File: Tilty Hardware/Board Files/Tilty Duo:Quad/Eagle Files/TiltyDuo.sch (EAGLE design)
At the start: 36 parts, among them U1 HMC5883LSMD, U2 HC-09_BREAKOUT, U3 MPL3115A2LGA8, U4 LM2931, U5 MPU-6050

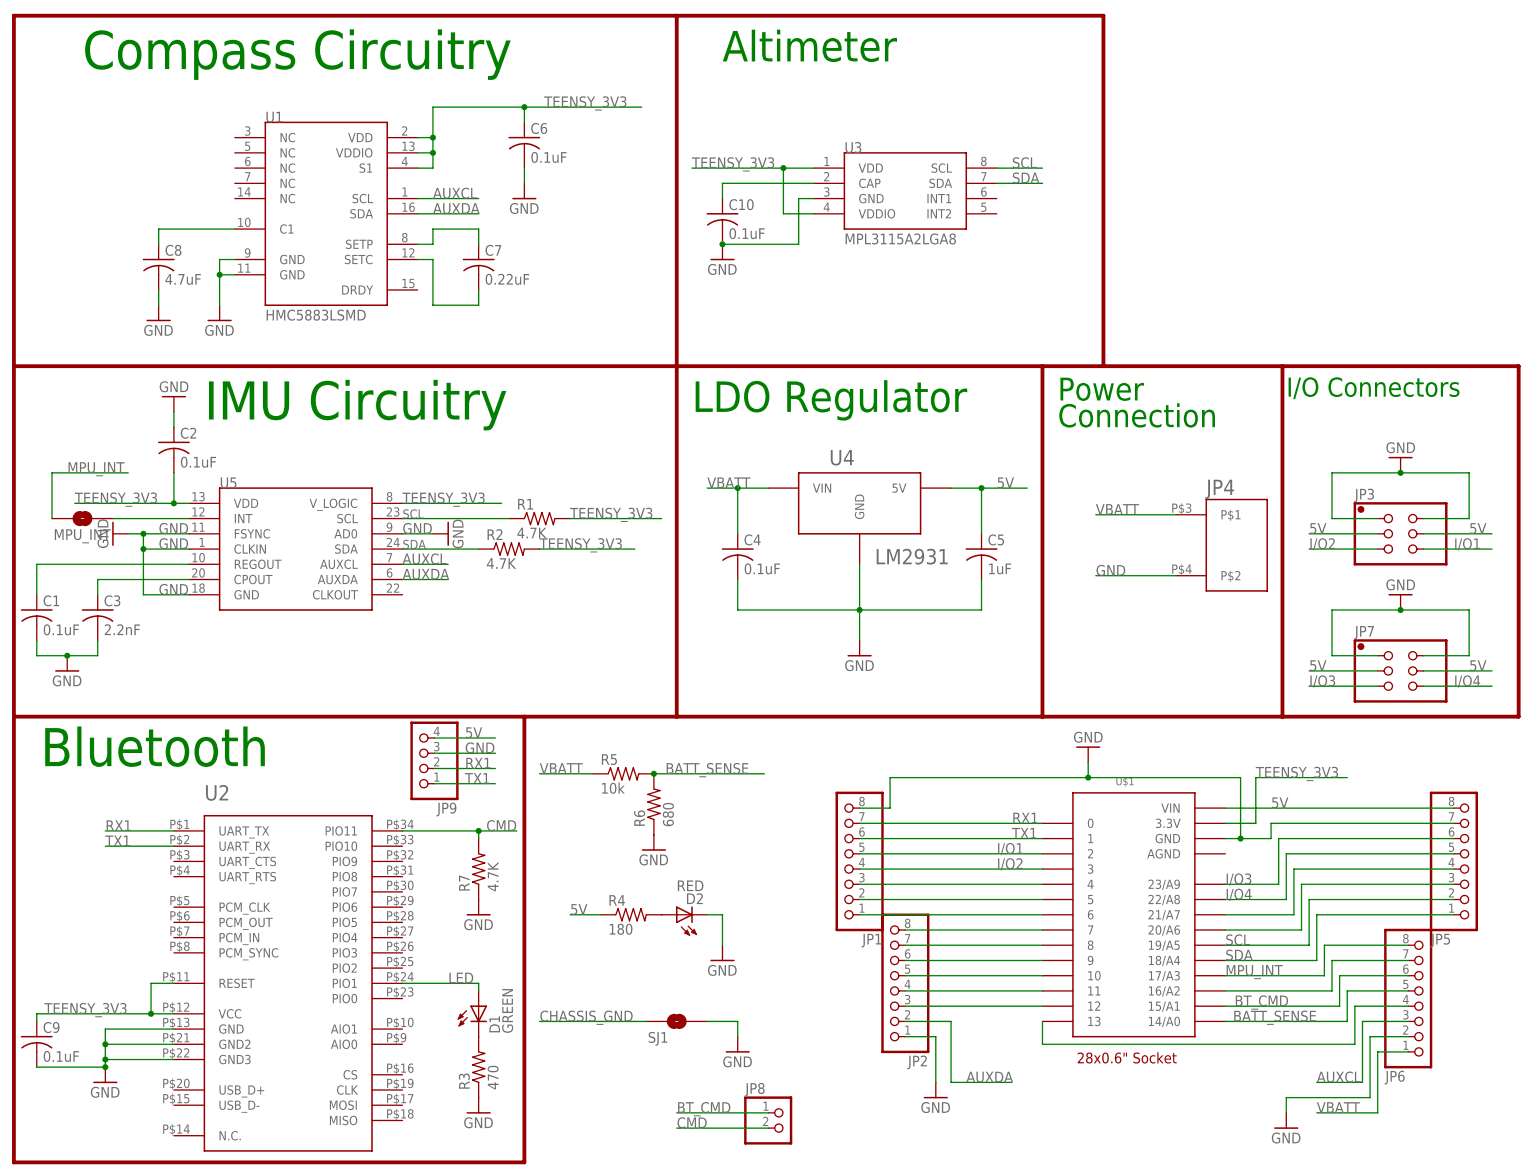
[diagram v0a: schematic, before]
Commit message: Added Bottom layer solder stencil for Duo/Quad board
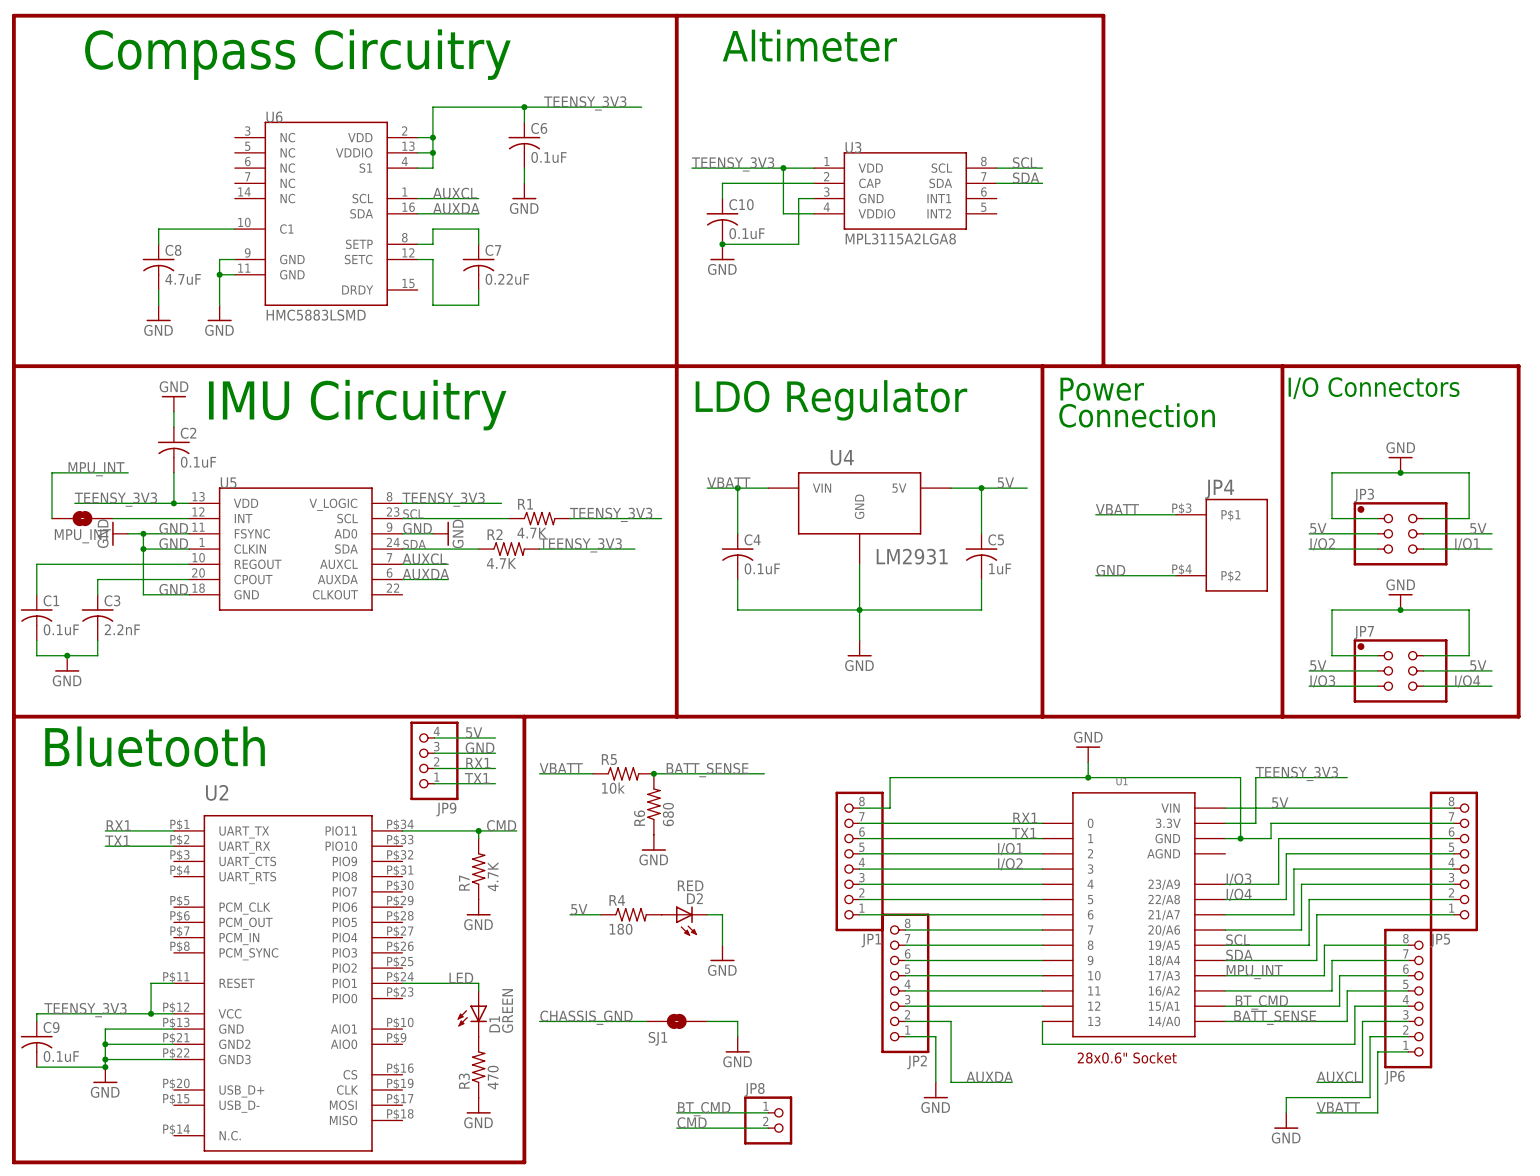
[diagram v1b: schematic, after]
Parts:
- removed U$1: TEENSY_3.0_OUTER-PINS28-DIP_SOCKET, My Parts:TEENSY_3.0_OUTER-PINS28-DIP_SOCKET
- added U6: HMC5883LSMD, SparkFun:HMC5883LSMD
- U1: value HMC5883LSMD -> TEENSY_3.0_OUTER-PINS28-DIP_SOCKET; device SparkFun:HMC5883LSMD -> My Parts:TEENSY_3.0_OUTER-PINS28-DIP_SOCKET; COST (none) -> 0.28
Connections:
- net 5V: now also U1.VIN; no longer U$1.VIN
- net AUXCL: now also U6.SCL; no longer U1.SCL
- net AUXDA: now also U6.SDA; no longer U1.SDA
- net BATT_SENSE: now also U1.14/A0; no longer U$1.14/A0
- net BT_CMD: now also U1.15/A1; no longer U$1.15/A1
- net GND: now also U1.GND, U6.GND@1, U6.GND@2; no longer U$1.GND, U1.GND@1, U1.GND@2
- net I/O1: now also U1.2; no longer U$1.2
- net I/O2: now also U1.3; no longer U$1.3
- net I/O3: now also U1.23/A9; no longer U$1.23/A9
- net I/O4: now also U1.22/A8; no longer U$1.22/A8
- net MPU_INT: now also U1.17/A3; no longer U$1.17/A3
- net N$10: now also U1.13; no longer U$1.13
- net N$11: now also U6.C1; no longer U1.C1
- net N$12: now also U1.9; no longer U$1.9
- net N$13: now also U1.10; no longer U$1.10
- net N$14: now also U1.11; no longer U$1.11
- net N$15: now also U1.12; no longer U$1.12
- net N$18: now also U1.21/A7; no longer U$1.21/A7
- net N$19: now also U1.20/A6; no longer U$1.20/A6
- net N$23: now also U1.16/A2; no longer U$1.16/A2
- net N$5: now also U6.SETP; no longer U1.SETP
- net N$6: now also U6.SETC; no longer U1.SETC
- net N$7: now also U1.4; no longer U$1.4
- net N$8: now also U1.5; no longer U$1.5
- net N$9: now also U1.6; no longer U$1.6
- net RX1: now also U1.0; no longer U$1.0
- net RX3: now also U1.7; no longer U$1.7
- net SCL: now also U1.19/A5; no longer U$1.19/A5
- net SDA: now also U1.18/A4; no longer U$1.18/A4
- net TEENSY_3V3: now also U1.3.3V, U6.S1, U6.VDD, U6.VDDIO; no longer U$1.3.3V, U1.S1, U1.VDD, U1.VDDIO
- net TX1: now also U1.1; no longer U$1.1
- net TX3: now also U1.8; no longer U$1.8
